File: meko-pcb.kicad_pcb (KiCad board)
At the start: 4 copper layers, 37 x 69 mm, 171 parts, among them IC1 AS5600-ASOM, IC2 TCAL9538RSVR, IC3 LP5912-3.3DRVR, IC4 ES9218PQ, IC5 BQ27427YZFR, J1 GDEY0154D67, J2 MEM2090-00-145-00-A, J3 USB_C_Receptacle_USB2.0_16P, J4 SJ2-35954B-SMT-TR, M1 HD-EMB1204-SM, Q1 SS8050, Q2 SS8050, Q3 SS8050, Q4 Si1308EDL, SW1 SW_Push, SW2 SW_Push, SW3 SW_Push, SW4 SW_Push, SW5 SW_Push, SW6 SW_Push, SW7 SW_Push, U1 ESP32-PICO-MINI-02, U10 LP5907SNX-1.8/NOPB, U2 BQ24075RGT, U3 LP5907SNX-3.3/NOPB, U4 LP5907SNX-3.3/NOPB, U5 LP5907SNX-1.8/NOPB, U6 LP5907SNX-3.3/NOPB, U7 LP5907SNX-1.8/NOPB, U8 USBLC6-2SC6, U9 CP2102N-Axx-xQFN24, Y1 ECS-2520SMV-500-GP-TR

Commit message: layout
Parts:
- removed JP4, JP5: SolderJumper_2_Bridged, Jumper:SolderJumper-2_P1.3mm_Bridged_RoundedPad1.0x1.5mm
- removed TP11, TP7: TestPoint, TestPoint:TestPoint_Pad_D1.5mm
- added C60: 4.7uF, Capacitor_SMD:C_0402_1005Metric, F.Cu at (60.8, 60.7)
- added C61: 100nF, Capacitor_SMD:C_0402_1005Metric, F.Cu at (60.8, 62.7)
- added D14: LED, LED_SMD:LED_0201_0603Metric, F.Cu at (65.7, 62.6)
- added R32: 1.5k, Resistor_SMD:R_0402_1005Metric, F.Cu at (65.7, 60.7)
- C42: footprint Capacitor_SMD:C_0402_1005Metric -> Capacitor_SMD:C_0603_1608Metric
- D2, JP1, JP10, JP3, JP6, JP7, JP8, JP9, Q1, Q2: moved to F.Cu
- moved D3 376.7 mm to (130.4, 59.3)
- moved D4 376.7 mm to (130.4, 55.9)
- moved JP2 376.7 mm to (135.5, 59.6)
- moved L1 376.7 mm to (135.8, 62.8)
- moved Q4 376.7 mm to (131.1, 63.0)
- moved D13 359.8 mm to (139.2, 78.9)
- moved D5 359.8 mm to (136.6, 42.4)
- moved JP10 326.0 mm to (94.3, 39.8), turned to 0 degrees
- moved D1 325.5 mm to (103.6, 81.3), turned to 90 degrees
- moved Q1 293.5 mm to (135.3, 51.2), turned to -90 degrees
- moved Q2 288.6 mm to (130.7, 51.2), turned to -90 degrees
- moved JP1 280.4 mm to (134.2, 68.4), turned to 0 degrees
- moved JP7 268.2 mm to (95.4, 32.5), turned to -90 degrees
- moved JP9 265.5 mm to (82.7, 41.2), turned to 90 degrees
- moved JP8 264.9 mm to (92.2, 32.5), turned to 90 degrees
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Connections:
- J3 pad S1: unconnected-(J3-SHIELD-PadS1)_3 -> GND
- U2 pad 6: Net-(JP4-B) -> +5V
- U3 pad 3: /power/EN3V3MCLK -> /power/REG-OUT
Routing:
- net /audio/C1: track 0.00 -> 3.14 mm
- net /audio/C1_VC: track 0.00 -> 1.81 mm
- net Net-(IC4-IN_L): track 0.00 -> 1.33 mm

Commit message: more layout
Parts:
- removed C30, C35, C37, C39: 1uF, Capacitor_SMD:C_0402_1005Metric
- C1, C2, C3, C4, C5, R1, R2, R3, R4, R5: moved to F.Cu
- moved C4 105.4 mm to (106.1, 33.6), turned to 90 degrees
- moved C5 104.0 mm to (106.2, 71.0), turned to 90 degrees
- moved C3 103.4 mm to (106.1, 46.3), turned to 90 degrees
- moved C48 97.7 mm to (94.7, 33.6)
- moved R4 96.5 mm to (106.1, 35.6), turned to 90 degrees
- moved R5 95.7 mm to (106.2, 73.0), turned to 90 degrees
- moved C49 95.3 mm to (93.9, 39.6), turned to -90 degrees
- moved C47 95.3 mm to (92.9, 33.6)
- moved R3 94.5 mm to (106.1, 48.2), turned to 90 degrees
- moved C50 87.3 mm to (83.0, 35.6), turned to -90 degrees
- moved C1 81.0 mm to (80.5, 25.8)
- moved C2 77.8 mm to (77.8, 73.0), turned to -90 degrees
- moved R1 74.6 mm to (82.5, 25.8)
- moved R2 68.9 mm to (77.8, 71.0), turned to -90 degrees
- moved IC2 24.8 mm to (103.7, 40.5), turned to -90 degrees
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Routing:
- net /audio/C1: track 3.14 -> 0.00 mm
- net /audio/C1_VC: track 1.81 -> 0.00 mm

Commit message: more layout
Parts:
- removed C59: 1uF, Capacitor_SMD:C_0402_1005Metric
- C11, C12, C14, C17, C18, C19, C20, C21, C22, D3, D4, JP2, L1, R12: moved to F.Cu
- C33: value 1uF -> 4.7uF
- D14: footprint LED_SMD:LED_0201_0603Metric -> LED_SMD:LED_0603_1608Metric; moved to B.Cu
- D6, D7, D8: footprint Package_DFN_QFN:Diodes_UDFN3810-9_TYPE_B -> Diodes_UDFN3810-9_TYPE_B-better-pinout:Diodes_UDFN3810-9_TYPE_B-better-pinout
- R32: moved to B.Cu
- moved C26 188.3 mm to (83.1, 74.7), turned to 0 degrees
- moved R16 182.2 mm to (86.2, 79.6)
- moved R31 134.4 mm to (78.9, 75.8)
- moved R20 125.8 mm to (86.6, 78.7), turned to 0 degrees
- moved C23 125.6 mm to (86.1, 76.3), turned to -90 degrees
- moved C24 125.2 mm to (83.1, 80.6), turned to 0 degrees
- moved R17 123.9 mm to (86.6, 77.7), turned to 0 degrees
- moved C25 123.3 mm to (83.1, 73.8), turned to 0 degrees
- moved R19 121.7 mm to (84.5, 75.0), turned to 90 degrees
- moved C15 105.3 mm to (101.6, 39.2), turned to -90 degrees
- moved JP1 103.6 mm to (31.1, 58.1)
- moved C22 103.5 mm to (97.9, 56.2), turned to 90 degrees
- moved C19 103.2 mm to (97.5, 53.0)
- moved C20 103.1 mm to (97.5, 53.9)
- moved C21 103.1 mm to (97.5, 54.8)
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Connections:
- C15 pad 1: Net-(IC2-VCC) -> GND
- C19 pad 2: Net-(J1-VSH1) -> /DISPL_VSH1
- D6 pad 4: /DISPL_~{CS} -> /DISPL_~{RES}
- D6 pad 5: /DISPL_~{D/C} -> /DISPL_BUSY
- D6 pad 6: /DISPL_~{RES} -> /DISPL_TSDA
- D6 pad 7: /DISPL_BUSY -> /DISPL_TSCL
- D7 pad 1: /DISPL_TSCL -> /DISPL_VCOM
- D7 pad 2: /DISPL_VPP -> /DISPL_PREVGL
- D7 pad 4: /DISPL_VCOM -> /DISPL_PREVSL
- D7 pad 5: /DISPL_PREVGL -> /DISPL_PREVGH
- D7 pad 6: /DISPL_PREVSL -> /DISPL_VSH1
- D7 pad 7: /DISPL_PREVGH -> /DISPL_VPP
- IC2 pad 14: Net-(IC2-VCC) -> +3V3
- J1 pad 20: Net-(J1-VSH1) -> /DISPL_VSH1
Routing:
- net +3V3VCCA: track 0.00 -> 4.34 mm
- net +3V3AVCC: track 0.00 -> 3.90 mm
- net /audio/C1: track 0.00 -> 3.51 mm
- net /audio/C2: track 0.00 -> 3.48 mm
- net /audio/PNEG: track 0.00 -> 3.15 mm
- net +1V8AVCC: track 0.00 -> 3.11 mm
- net /audio/PNEG_VC: track 0.00 -> 2.32 mm
- net /audio/C2_VC: track 0.00 -> 2.08 mm
- net /audio/C1_VC: track 0.00 -> 2.03 mm
- net GND: vias 0 -> 93

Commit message: almost finished with the layout
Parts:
- removed D13: MBR0530, Diode_SMD:D_SOD-123
- C10, C13, C16, C9, D5, R7, R8: moved to F.Cu
- C60, C61: moved to B.Cu
- R30: value 47k -> 100k; moved to F.Cu
- moved R26 166.5 mm to (94.2, 80.0), turned to 90 degrees
- moved R25 163.3 mm to (89.8, 80.0), turned to 90 degrees
- moved SW6 136.7 mm to (103.1, 78.6), turned to 90 degrees
- moved SW7 133.2 mm to (98.5, 78.7), turned to 90 degrees
- moved C32 124.9 mm to (108.7, 24.7), turned to 0 degrees
- moved C31 123.5 mm to (109.0, 27.6), turned to 0 degrees
- moved C40 115.1 mm to (97.6, 79.9), turned to -90 degrees
- moved R22 109.7 mm to (97.0, 73.5)
- moved R21 101.8 mm to (88.4, 73.8), turned to 0 degrees
- moved R23 101.6 mm to (89.7, 70.3), turned to 0 degrees
- moved R24 101.1 mm to (89.7, 69.2), turned to 0 degrees
- moved R35 100.4 mm to (95.3, 24.9)
- moved C10 97.6 mm to (96.2, 73.1), turned to -90 degrees
- moved R10 97.6 mm to (106.3, 52.1)
- moved R11 97.6 mm to (106.3, 54.1)
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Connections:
- M1 pad SH1: unconnected-(M1-SHIELD-PadSH1) -> GND
- Q2 pad 3: Net-(D13-A) -> /BOOT
- R27 pad 1: +3V3AVDD -> +3V3
- R30 pad 1: /AUDIO_DATA_CLK/BOOT -> +3V3
- R30 pad 2: GND -> /AUDIO_DATA_CLK/BOOT
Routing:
- net /audio/DVDD: track 0.00 -> 1.63 mm
- net GND: vias 93 -> 90

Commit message: more routing
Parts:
- added C30: 100nF, Capacitor_SMD:C_0402_1005Metric, F.Cu at (76.4, 45.3)
- C6, C7, R10, R11, R6: moved to F.Cu
- moved C6 105.2 mm to (106.7, 77.0), turned to -90 degrees
- moved C7 98.9 mm to (95.2, 76.8), turned to -90 degrees
- moved R6 95.4 mm to (105.5, 77.0), turned to 90 degrees
- moved TP10 78.2 mm to (-5.20, 112.0)
- moved D2 22.1 mm to (74.8, 45.3), turned to 180 degrees
- moved R35 14.1 mm to (104.9, 35.3), turned to 0 degrees
- moved R29 7.16 mm to (94.2, 52.2)
- moved R28 5.43 mm to (97.7, 52.3), turned to 0 degrees
- moved R33 5.01 mm to (77.5, 38.5), turned to 180 degrees
- moved R24 3.15 mm to (92.8, 70.1), turned to -90 degrees
- moved R11 2.75 mm to (104.0, 52.5)
- moved R22 2.62 mm to (97.4, 70.9)
- moved R30 2.40 mm to (96.3, 76.9), turned to 90 degrees
- moved R10 2.29 mm to (104.6, 50.6)
- moved JP6 2.16 mm to (79.5, 36.8)
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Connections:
- C25 pad 2: /power/REG-OUT -> REG-OUT
- C26 pad 2: /power/REG-OUT -> REG-OUT
- C27 pad 1: /power/REG-OUT -> REG-OUT
- C29 pad 1: /power/REG-OUT -> REG-OUT
- C31 pad 1: +3V3 -> REG-OUT
- C34 pad 1: /power/REG-OUT -> REG-OUT
- C38 pad 1: +3V3 -> REG-OUT
- IC3 pad 4: /power/REG-OUT -> REG-OUT
- IC3 pad 6: /power/REG-OUT -> REG-OUT
- IC5 pad C2: /power/REG-OUT -> REG-OUT
- JP10 pad 1: +3V3 -> REG-OUT
- JP6 pad 1: /power/REG-OUT -> REG-OUT
- JP7 pad 1: /power/REG-OUT -> REG-OUT
- Q2 pad 3: /BOOT -> /AUDIO_DATA_CLK/BOOT
- U10 pad 4: +3V3 -> REG-OUT
- U2 pad 10: /power/REG-OUT -> REG-OUT
- U2 pad 11: /power/REG-OUT -> REG-OUT
- U3 pad 3: /power/REG-OUT -> REG-OUT
- U3 pad 4: /power/REG-OUT -> REG-OUT
- U4 pad 4: /power/REG-OUT -> REG-OUT
- U5 pad 3: +3V3 -> REG-OUT
- U5 pad 4: +3V3 -> REG-OUT
- U6 pad 4: /power/REG-OUT -> REG-OUT
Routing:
- net +3V3: track 0.00 -> 283.7 mm, vias 0 -> 29
- net GND: track 0.00 -> 177.9 mm, vias 90 -> 244
- net REG-OUT: track 0.00 -> 140.8 mm, vias 0 -> 12
- net /I2C_SDA: track 0.00 -> 90.0 mm, vias 0 -> 5
- net /I2C_SCL: track 0.00 -> 88.6 mm, vias 0 -> 5
- net /BTN_PWR: track 0.00 -> 66.8 mm, vias 0 -> 7
- net /AUDIO_DATA_CLK/BOOT: track 0.00 -> 56.3 mm, vias 0 -> 3
- net /PWR_EN3V3VCCA: track 0.00 -> 54.5 mm, vias 0 -> 3
- net /AUDIO_MLCK_EN: track 0.00 -> 53.9 mm, vias 0 -> 2
- net /BTN_VOL_UP: track 0.00 -> 52.9 mm, vias 0 -> 7
- net /MEM_DAT0: track 0.00 -> 46.8 mm
- net /MEM_CMD: track 0.00 -> 43.2 mm, vias 0 -> 2
- net /MEM_DAT2: track 0.00 -> 41.3 mm, vias 0 -> 2
- net /MEM_DAT1: track 0.00 -> 40.9 mm
- net /BTN_SIDE_L: track 0.00 -> 37.9 mm, vias 0 -> 1
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
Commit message: finished routing
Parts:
- removed C31, C32: 1uF, Capacitor_SMD:C_0402_1005Metric
- removed R34: 1.8k, Resistor_SMD:R_0402_1005Metric
- removed TP12, TP14, TP15, TP5, TP8, TP9: TestPoint, TestPoint:TestPoint_Pad_D1.5mm
- removed U5: LP5907SNX-1.8/NOPB, Package_SON:Texas_X2SON-4_1x1mm_P0.65mm
- added TP21: TestPoint, TestPoint:TestPoint_Pad_D1.0mm, F.Cu at (92.5, 63.8)
- added TP22: TestPoint, TestPoint:TestPoint_Pad_D1.0mm, B.Cu at (91.4, 55.4)
- R33: moved to F.Cu
- TP1, TP16, TP17, TP3, TP4: footprint TestPoint:TestPoint_Pad_D1.5mm -> TestPoint:TestPoint_Pad_D1.0mm
- TP10, TP13, TP18, TP19, TP2, TP20, TP6: footprint TestPoint:TestPoint_Pad_D1.5mm -> TestPoint:TestPoint_Pad_D1.0mm; moved to F.Cu
- moved TP19 122.7 mm to (103.9, 49.0)
- moved TP20 122.3 mm to (101.7, 49.3)
- moved TP18 118.3 mm to (94.6, 40.6)
- moved TP16 116.5 mm to (89.8, 30.4)
- moved TP4 112.0 mm to (96.1, 73.4)
- moved TP6 109.8 mm to (93.5, 76.6)
- moved TP1 109.5 mm to (94.8, 70.5)
- moved TP3 109.4 mm to (95.4, 76.3)
- moved TP13 107.6 mm to (85.0, 37.9)
- moved TP2 106.4 mm to (84.8, 65.8)
- moved TP10 94.6 mm to (82.8, 77.4)
- moved TP17 89.3 mm to (80.7, 69.7)
- moved D12 23.1 mm to (104.5, 36.3)
- moved D11 18.7 mm to (97.3, 32.6), turned to 0 degrees
- moved D10 12.8 mm to (97.3, 28.0), turned to -90 degrees
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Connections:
- C41 pad 2: /AUDIO_RESETB -> /AUDIO_DISPL_RESETB
- D6 pad 4: /DISPL_~{RES} -> /AUDIO_DISPL_RESETB
- D9 pad 2: /AUDIO_MIC -> Net-(D9-A2)
- IC2 pad 8: /AUDIO_RESETB -> /AUDIO_DISPL_RESETB
- IC4 pad 37: /AUDIO_RESETB -> /AUDIO_DISPL_RESETB
- J1 pad 10: /DISPL_~{RES} -> /AUDIO_DISPL_RESETB
- J4 pad S: /AUDIO_MIC -> Net-(D9-A2)
- R27 pad 2: /AUDIO_RESETB -> /AUDIO_DISPL_RESETB
- U1 pad 6: /AUDIO_MIC -> /DISPL_BUSY
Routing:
- net /PWR_FUEL_GPOUT: track 13.6 -> 71.0 mm, vias 1 -> 10
- net /AUDIO_DISPL_RESETB: track 0.00 -> 52.2 mm, vias 0 -> 6
- net /EXP_~{INT}: track 2.22 -> 42.6 mm, vias 0 -> 4
- net /AUDIO_RESETB: track 36.2 -> 0.00 mm, vias 4 -> 0
- net /EXP_~{RES}: track 1.27 -> 27.5 mm, vias 0 -> 4
- net /DISPL_BUSY: track 2.72 -> 28.3 mm, vias 0 -> 3
- net GND: track 177.9 -> 191.6 mm, vias 244 -> 260
- net /USB/~{SUSP}: track 1.27 -> 12.9 mm, vias 0 -> 3
- net +1V8AVCC: track 4.19 -> 11.3 mm, vias 0 -> 2
- net /AUDIO_MLCK_EN: track 53.9 -> 58.1 mm
- net Net-(D9-A2): track 0.00 -> 3.64 mm
- net /DISPL_~{RES}: track 3.57 -> 0.00 mm
- net REG-OUT: track 140.8 -> 144.1 mm
- net /AUDIO_MIC: track 3.12 -> 0.00 mm
- net /PWR_EN1V8AVCC: track 19.8 -> 22.7 mm
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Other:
- outline, holes or cut-outs redrawn

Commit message: minor stuff
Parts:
- added H1: MountingHole, MountingHole:MountingHole_2.2mm_M2, F.Cu at (82.7, 32.8)
- added H2: MountingHole, MountingHole:MountingHole_2.2mm_M2, F.Cu at (107.8, 52.8)
- added H3: MountingHole, MountingHole:MountingHole_2.2mm_M2, F.Cu at (87.6, 81.7)
- added H4: MountingHole, MountingHole:MountingHole_2.2mm_M2, F.Cu at (108.3, 78.8)
- moved C24 3.17 mm to (79.9, 80.4)
- moved C6 2.26 mm to (105.5, 75.0), turned to 90 degrees
- moved R18 0.74 mm to (81.8, 80.6), turned to 0 degrees
- moved C57 0.16 mm to (78.0, 79.7)
- moved C58 0.16 mm to (78.0, 80.6)
- moved R16 0.13 mm to (86.3, 79.6)
- moved J4 0.12 mm to (102.5, 27.9)
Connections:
- IC5 pad C2: REG-OUT -> /power/SRX
- U2 pad 2: +BATT -> /power/SRX
- U2 pad 3: +BATT -> /power/SRX
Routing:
- net /power/SRX: track 0.00 -> 8.27 mm, vias 0 -> 2
- net REG-OUT: track 144.1 -> 137.8 mm
- net +3V3: track 284.3 -> 280.9 mm, vias 28 -> 27
- net +BATT: track 11.3 -> 9.29 mm
- net Net-(D9-A2): track 3.64 -> 3.02 mm
- net /AUDIO_MLCK_EN: track 58.1 -> 58.7 mm
- net /PWR_EN_USB: track 23.0 -> 23.5 mm
- net GND: track 191.6 -> 191.5 mm, vias 260 -> 259

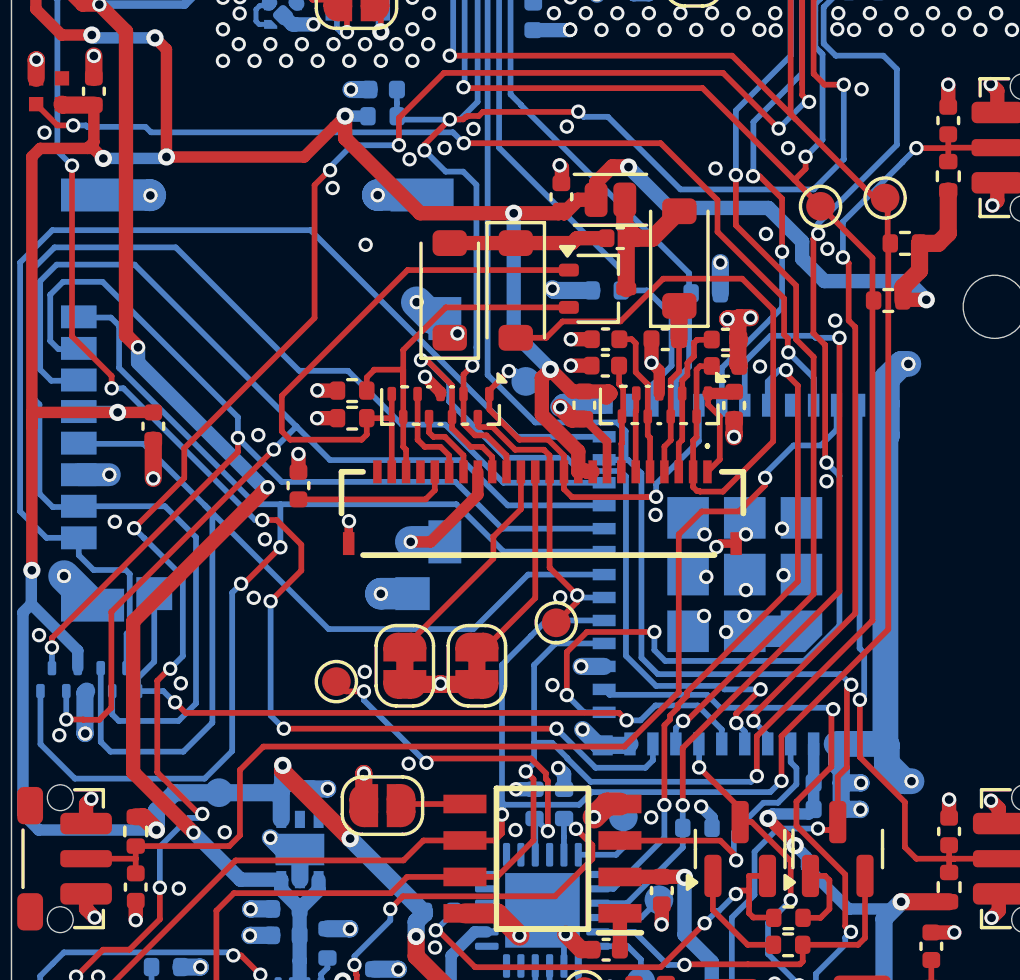
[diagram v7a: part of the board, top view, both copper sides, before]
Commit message: added test points to uart
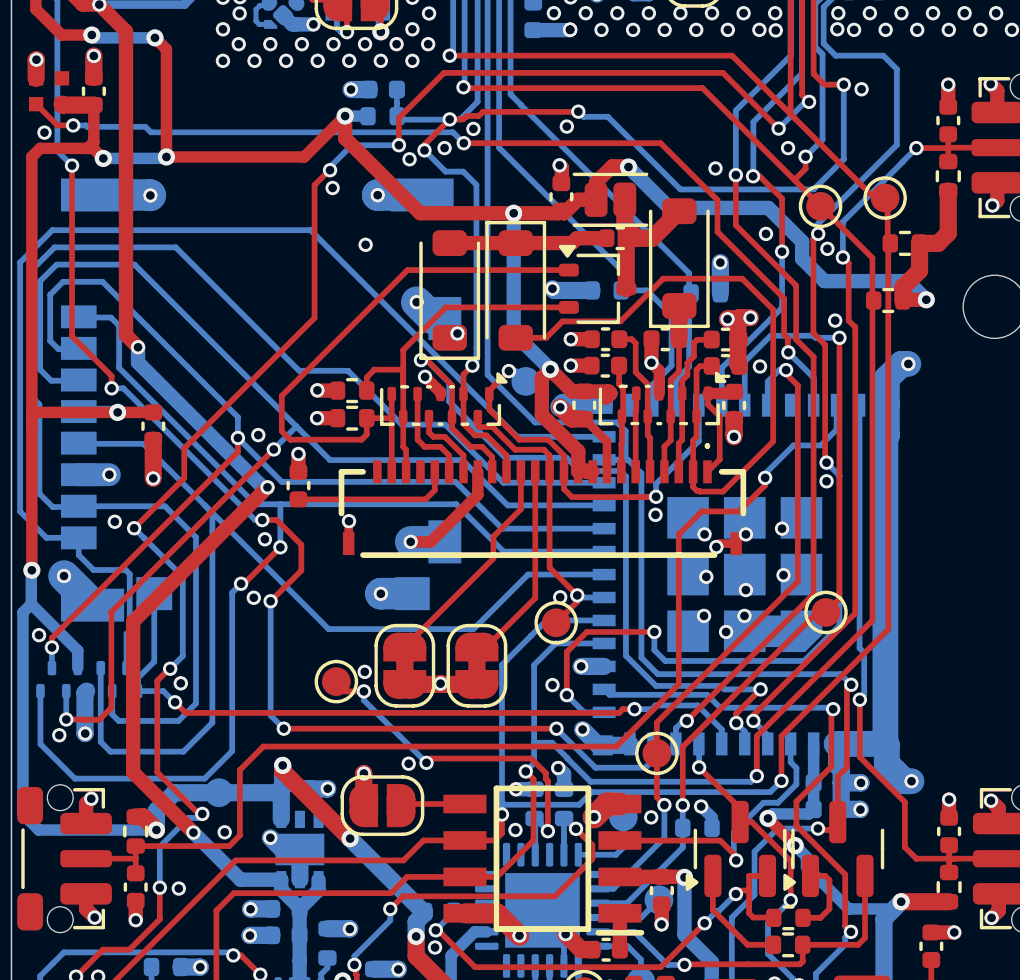
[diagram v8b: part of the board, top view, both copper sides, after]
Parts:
- added TP5: TestPoint, TestPoint:TestPoint_Pad_D1.0mm, F.Cu at (101.9, 63.4)
- added TP7: TestPoint, TestPoint:TestPoint_Pad_D1.0mm, F.Cu at (96.0, 68.3)
